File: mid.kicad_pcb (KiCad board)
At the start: 2 copper layers, 99.1 x 49.9 mm, 27 parts, among them P1 POLOLU_MICROSD1, P2 ADAFRUIT_MICROSD1, P3 EBAY_MICROSD1, P4 POLOLU_MICROSD2, P5 ADAFRUIT_MICROSD2, P6 EBAY_MICROSD2, P7 SPI, P8 RC2014_STANDARD_DEV_39, SW1 SW_DIP_x04, U1 TP3465-PLCC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

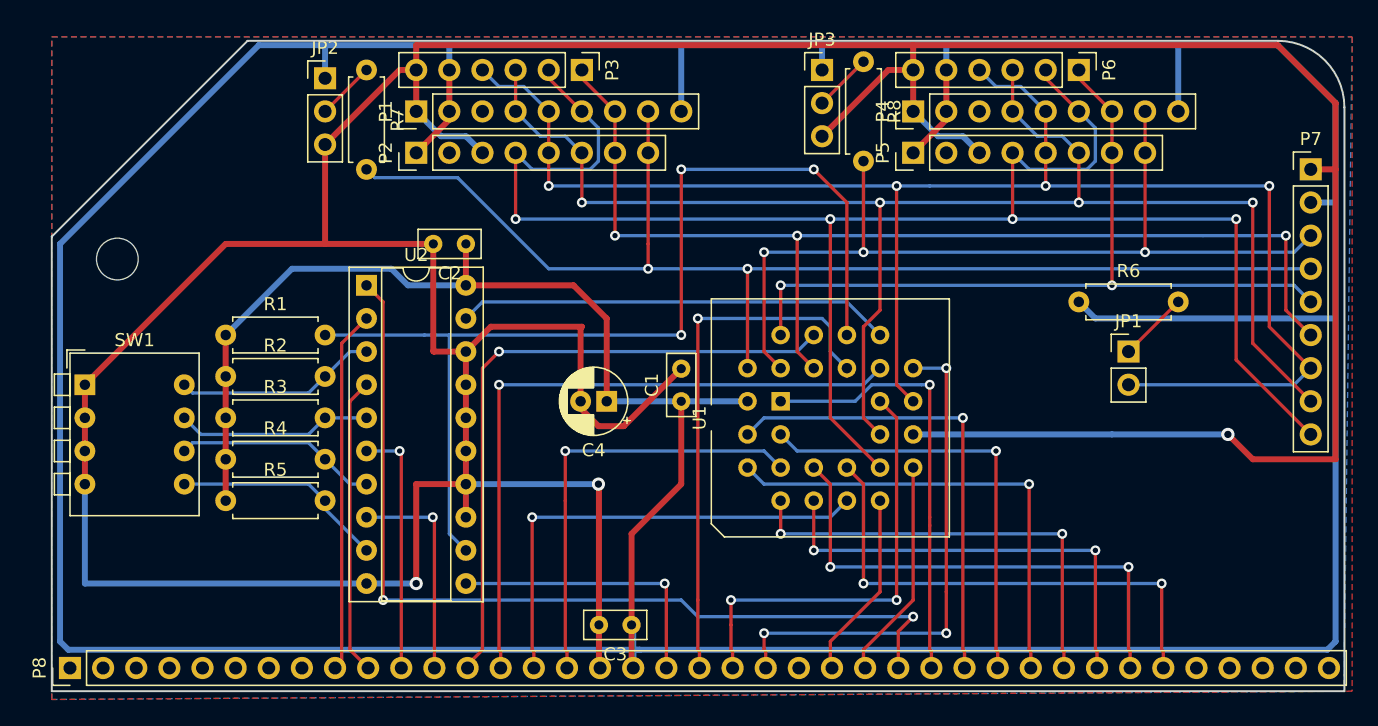
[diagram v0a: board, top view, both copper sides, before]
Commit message: adjust position of R8 & JP3  allows GND and VCC to be moved away from the top edge of the board
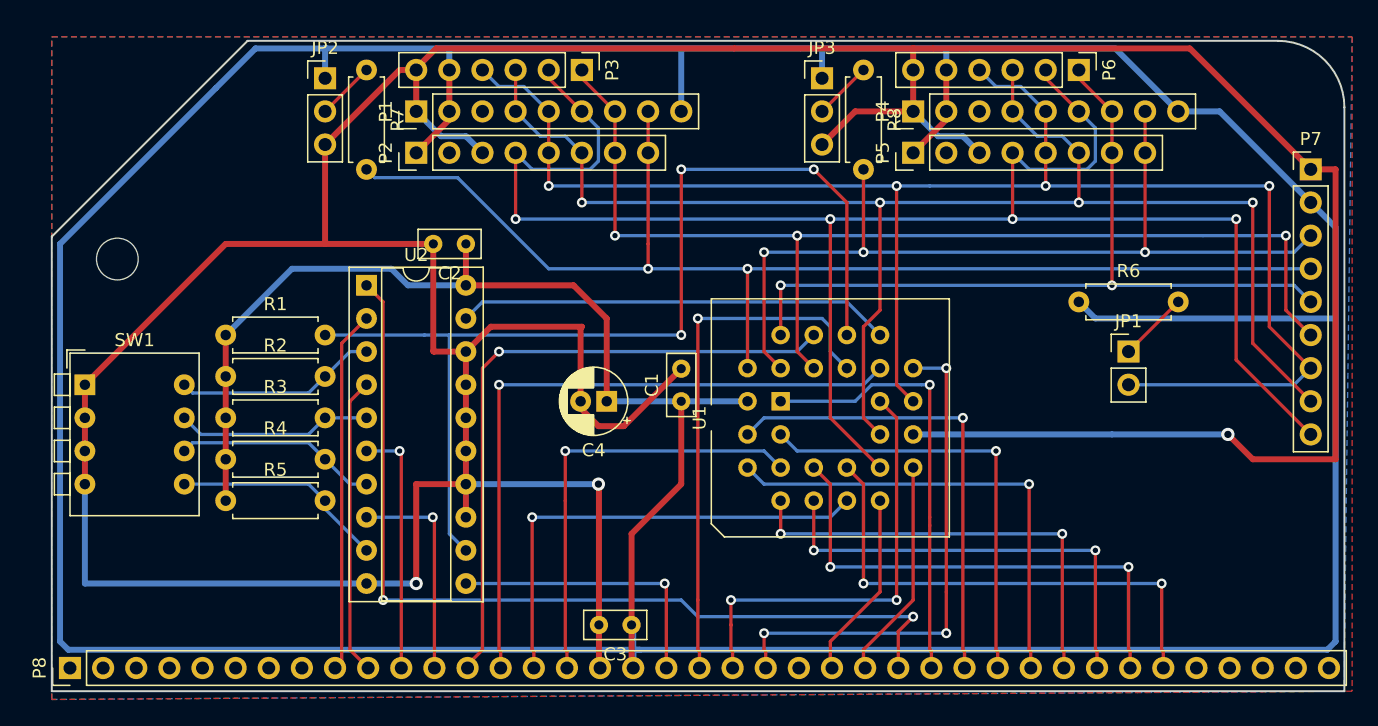
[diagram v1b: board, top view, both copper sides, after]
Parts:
- moved R8 0.64 mm to (151.1, 90.8)
- moved JP3 0.63 mm to (148.0, 91.4)
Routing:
- net VCC: track 425.4 -> 412.4 mm
- net GND: track 340.8 -> 333.8 mm

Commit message: add silkscreen layers
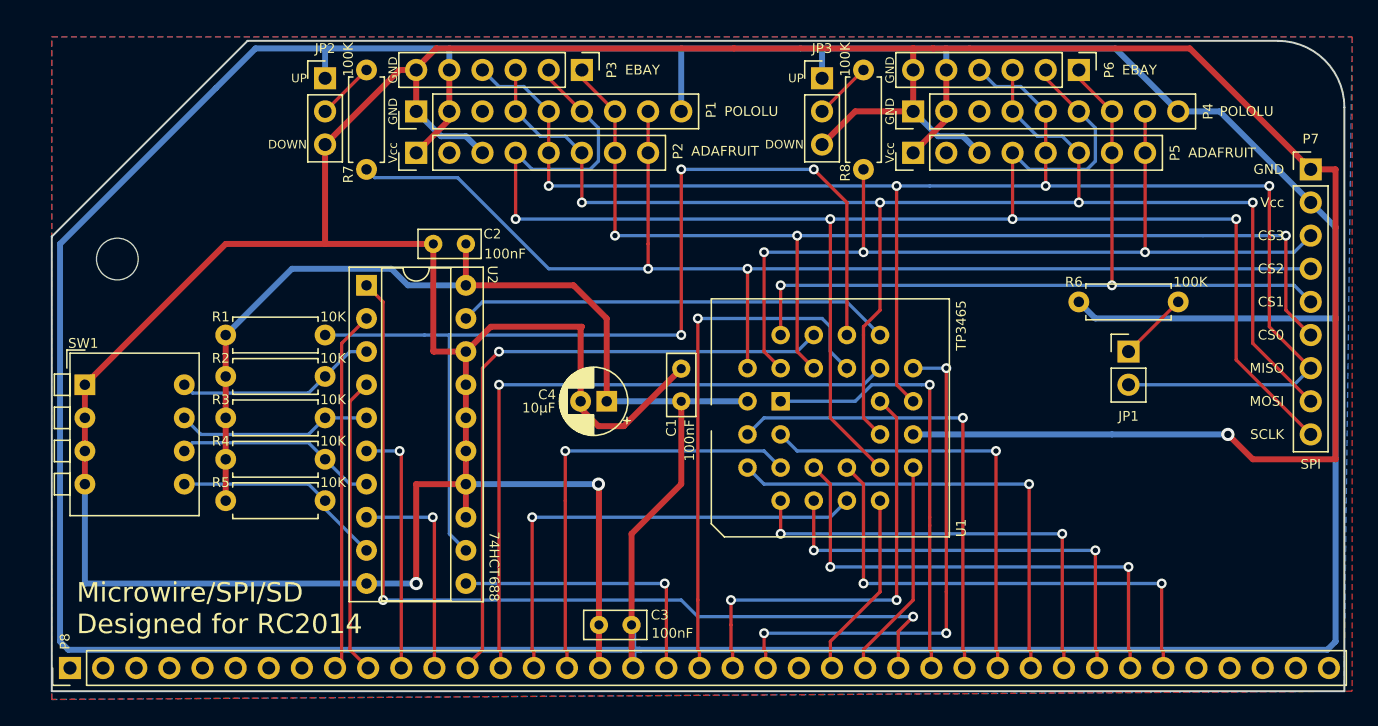
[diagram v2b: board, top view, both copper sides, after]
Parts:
- R6, R7, R8: value 10K -> 100K
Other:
- board text added: "100K"
- board text added: "100nF"
- board text added: "10K"
- board text added: "10µF"
- board text added: "20200420 ©2020 Chris Odorjan https://github.com/codorjan/rc_mid"
- board text added: "74HCT688"
- board text added: "ADAFRUIT"
- board text added: "CS0"
- board text added: "CS1"
- board text added: "CS2"
- board text added: "CS3"
- board text added: "Close JP1 to enable a 100K pull-up on the MISO line. This is required but most SD adapters omit it. (The Pololu adapter is known to have it.) This pull-up is likely unnecessary as most software (e.g. RomWBW) include a workaround but is here just in case it's helpful."
- board text added: "DOWN"
- board text added: "EBAY"
- board text added: "GND"
- board text added: "JP1"
- board text added: "JP2"
- board text added: "JP2 and JP3 allow the card detect lines to be pulled- up or pulled-down as required to detect the presence of an SD card in each adapter. Leave these unpopulated if the generic SPI interface is being used. Like JP1 these are here in case they're helpful."
- board text added: "JP3"
- board text added: "MISO"
- board text added: "MOSI"
- board text added: "Microwire/SPI/SD Designed for RC2014"
- board text added: "POLOLU"
- board text added: "SCLK"
- board text added: "SPI"
- board text added: "SW1 = upper nibble of base address (on/dn = binary 0, off/up = binary 1)"
- board text added: "TP3465"
- board text added: "U1"
- board text added: "U2"
- board text added: "UP"
- board text added: "Vcc"
